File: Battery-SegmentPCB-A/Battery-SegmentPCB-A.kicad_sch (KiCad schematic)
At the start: 10 parts, among them J1 Conn_01x04, J10 Conn_01x16, J2 Conn_01x04, J3 Conn_01x04, J4 Conn_01x04, J5 Conn_01x04, J6 Conn_01x04, J7 Conn_01x04, J8 Conn_01x04, J9 Conn_01x09

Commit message: Initial commit
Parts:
- removed J10: Conn_01x16, footprints:CON_430451612_MOL, symbol Connector_Generic:Conn_01x16
- added J11: Conn_01x09, footprints:CON_436500915_MOL, symbol Connector_Generic:Conn_01x09
- J1, J2, J3, J4, J5, J6, J7, J8: footprint UTSVT_Connectors:Molex_MicroFit3.0_1x4xP3.00mm_PolarizingPeg_Vertical -> footprints:CONN_S4B-PH-K-S_JST
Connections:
- net VOLT1_1 +: now also J11.2 (Pin_2)
- net VOLT1_2 +: now also J11.3 (Pin_3)
- net VOLT1_3 +: now also J11.4 (Pin_4)
- net VOLT1_4 +: now also J11.5 (Pin_5)
- net VOLT1_5 +: now also J11.6 (Pin_6)
- net VOLT1_6 +: now also J11.7 (Pin_7)
- net VOLT1_7 +: now also J11.8 (Pin_8)
- net VOLT1_8 +: now also J11.9 (Pin_9)
- net VOLT_1 -: now also J11.1 (Pin_1)
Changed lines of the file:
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@@
-	(wire
-		(pts
-			(xy 137.16 60.96) (xy 137.16 64.77)
-		)
-		(stroke
-			(width 0)
-			(type default)
-		)
-	)
 	(wire
 		(pts
@@
 	(wire
 		(pts
-			(xy 132.08 60.96) (xy 132.08 64.77)
-		)
-		(stroke
-			(width 0)
-			(type default)
-		)
-	)
-	(wire
-		(pts
 			(xy 33.02 96.52) (xy 38.1 96.52)
 		)
@@
 	(wire
 		(pts
-			(xy 124.46 60.96) (xy 124.46 64.77)
-		)
-		(stroke
-			(width 0)
-			(type default)
-		)
-	)
-	(wire
-		(pts
 			(xy 33.02 62.23) (xy 38.1 62.23)
 		)
@@
 	(wire
 		(pts
-			(xy 139.7 60.96) (xy 139.7 64.77)
-		)
-		(stroke
-			(width 0)
-			(type default)
-		)
-	)
-	(wire
-		(pts
 			(xy 33.02 99.06) (xy 38.1 99.06)
 		)
@@
 	(wire
 		(pts
-			(xy 142.24 60.96) (xy 142.24 64.77)
-		)
-		(stroke
-			(width 0)
-			(type default)
-		)
-	)
-	(wire
-		(pts
-			(xy 134.62 60.96) (xy 134.62 64.77)
-		)
-		(stroke
-			(width 0)
-			(type default)
-		)
-	)
-	(wire
-		(pts
 			(xy 33.02 113.03) (xy 38.1 113.03)
 		)
@@
 	(wire
 		(pts
-			(xy 127 60.96) (xy 127 64.77)
-		)
-		(stroke
-			(width 0)
-			(type default)
-		)
-	)
-	(wire
-		(pts
 			(xy 119.38 60.96) (xy 119.38 64.77)
 		)
@@
 	(wire
 		(pts
-			(xy 129.54 60.96) (xy 129.54 64.77)
+			(xy 101.6 60.96) (xy 101.6 64.77)
 		)
 		(stroke
@@
 			(width 0)
 			(type default)
-		)
-	)
-	(label "VOLT_8 -"
-		(at 142.24 64.77 270)
-		(fields_autoplaced yes)
-		(effects
-			(font
-				(size 1.27 1.27)
-			)
-			(justify right bottom)
 		)
 	)
@@
 	)
 	(label "VOLT_1 -"
-		(at 124.46 64.77 270)
+		(at 101.6 64.77 270)
 		(fields_autoplaced yes)
 		(effects
@@
 		)
 	)
-	(label "VOLT_4 -"
-		(at 132.08 64.77 270)
-		(fields_autoplaced yes)
-		(effects
-			(font
-				(size 1.27 1.27)
-			)
-			(justify right bottom)
-		)
-	)
 	(label "VOLT1_5 +"
 		(at 33.02 78.74 180)
@@
 		)
 	)
-	(label "VOLT_5 -"
-		(at 134.62 64.77 270)
-		(fields_autoplaced yes)
-		(effects
-			(font
-				(size 1.27 1.27)
-			)
-			(justify right bottom)
-		)
-	)
 	(label "TEMP_7"
 		(at 33.02 96.52 180)
@@
 		)
 	)
-	(label "VOLT_3 -"
-		(at 129.54 64.77 270)
-		(fields_autoplaced yes)
-		(effects
-			(font
-				(size 1.27 1.27)
-			)
-			(justify right bottom)
-		)
-	)
 	(label "TEMP_6"
 		(at 33.02 85.09 180)
@@
 		)
 	)
-	(label "VOLT_7 -"
-		(at 139.7 64.77 270)
-		(fields_autoplaced yes)
-		(effects
-			(font
-				(size 1.27 1.27)
-			)
-			(justify right bottom)
-		)
-	)
-	(label "VOLT_2 -"
-		(at 127 64.77 270)
-		(fields_autoplaced yes)
-		(effects
-			(font
-				(size 1.27 1.27)
-			)
-			(justify right bottom)
-		)
-	)
 	(label "VOLT_4 -"
 		(at 33.02 59.69 180)
-		(fields_autoplaced yes)
-		(effects
-			(font
-				(size 1.27 1.27)
-			)
-			(justify right bottom)
-		)
-	)
-	(label "VOLT_6 -"
-		(at 137.16 64.77 270)
 		(fields_autoplaced yes)
 		(effects
@@
 			)
 		)
-		(property "Footprint" "UTSVT_Connectors:Molex_MicroFit3.0_1x4xP3.00mm_PolarizingPeg_Vertical"
+		(property "Footprint" "footprints:CONN_S4B-PH-K-S_JST"
 			(at 43.18 39.37 0)
 			(effects
@@
 			)
 		)
-		(property "Footprint" "UTSVT_Connectors:Molex_MicroFit3.0_1x4xP3.00mm_PolarizingPeg_Vertical"
+		(property "Footprint" "footprints:CONN_S4B-PH-K-S_JST"
 			(at 43.18 27.94 0)
 			(effects
@@
 			)
 		)
-		(property "Footprint" "UTSVT_Connectors:Molex_MicroFit3.0_1x4xP3.00mm_PolarizingPeg_Vertical"
+		(property "Footprint" "footprints:CONN_S4B-PH-K-S_JST"
 			(at 43.18 62.23 0)
 			(effects
@@
 				(path "/4c734560-430e-4436-a585-cee76e7030f6"
 					(reference "J4")
-					(unit 1)
-				)
-			)
-		)
-	)
-	(symbol
-		(lib_id "Connector_Generic:Conn_01x16")
-		(at 121.92 55.88 90)
-		(unit 1)
-		(exclude_from_sim no)
-		(in_bom yes)
-		(on_board yes)
-		(dnp no)
-		(fields_autoplaced yes)
-		(property "Reference" "J10"
-			(at 123.19 49.53 90)
-			(effects
-				(font
-					(size 1.27 1.27)
-				)
-			)
-		)
-		(property "Value" "Conn_01x16"
-			(at 123.19 52.07 90)
-			(effects
-				(font
-					(size 1.27 1.27)
-				)
-			)
-		)
-		(property "Footprint" "footprints:CON_430451612_MOL"
-			(at 121.92 55.88 0)
-			(effects
-				(font
-					(size 1.27 1.27)
-				)
-				(hide yes)
-			)
-		)
-		(property "Datasheet" "~"
-			(at 121.92 55.88 0)
-			(effects
-				(font
-					(size 1.27 1.27)
-				)
-				(hide yes)
-			)
-		)
-		(property "Description" "Generic connector, single row, 01x16, script generated (kicad-library-utils/schlib/autogen/connector/)"
-			(at 121.92 55.88 0)
-			(effects
-				(font
-					(size 1.27 1.27)
-				)
-				(hide yes)
-			)
-		)
-		(pin "16"
-		)
-		(pin "5"
-		)
-		(pin "9"
-		)
-		(pin "2"
-		)
-		(pin "4"
-		)
-		(pin "14"
-		)
-		(pin "6"
-		)
-		(pin "1"
-		)
-		(pin "11"
-		)
-		(pin "10"
-		)
-		(pin "8"
-		)
-		(pin "3"
-		)
-		(pin "13"
-		)
-		(pin "15"
-		)
-		(pin "7"
-		)
-		(pin "12"
-		)
-		(instances
-			(project "Battery-SegmentPCB-A"
-				(path "/4c734560-430e-4436-a585-cee76e7030f6"
-					(reference "J10")
 					(unit 1)
 				)
@@
 			)
 		)
-		(property "Footprint" "UTSVT_Connectors:Molex_MicroFit3.0_1x4xP3.00mm_PolarizingPeg_Vertical"
+		(property "Footprint" "footprints:CONN_S4B-PH-K-S_JST"
 			(at 43.18 107.95 0)
 			(effects
@@
 			)
 		)
-		(property "Footprint" "UTSVT_Connectors:Molex_MicroFit3.0_1x4xP3.00mm_PolarizingPeg_Vertical"
+		(property "Footprint" "footprints:CONN_S4B-PH-K-S_JST"
 			(at 43.18 50.8 0)
 			(effects
@@
 			)
 		)
-		(property "Footprint" "UTSVT_Connectors:Molex_MicroFit3.0_1x4xP3.00mm_PolarizingPeg_Vertical"
+		(property "Footprint" "footprints:CONN_S4B-PH-K-S_JST"
 			(at 43.18 96.52 0)
 			(effects
@@
 			)
 		)
-		(property "Footprint" "UTSVT_Connectors:Molex_MicroFit3.0_1x4xP3.00mm_PolarizingPeg_Vertical"
+		(property "Footprint" "footprints:CONN_S4B-PH-K-S_JST"
 			(at 43.18 73.66 0)
 			(effects
@@
 	)
 	(symbol
+		(lib_id "Connector_Generic:Conn_01x09")
+		(at 111.76 55.88 90)
+		(unit 1)
+		(exclude_from_sim no)
+		(in_bom yes)
+		(on_board yes)
+		(dnp no)
+		(fields_autoplaced yes)
+		(property "Reference" "J11"
+			(at 111.76 49.53 90)
+			(effects
+				(font
+					(size 1.27 1.27)
+				)
+			)
+		)
+		(property "Value" "Conn_01x09"
+			(at 111.76 52.07 90)
+			(effects
+				(font
+					(size 1.27 1.27)
+				)
+			)
+		)
+		(property "Footprint" "footprints:CON_436500915_MOL"
+			(at 111.76 55.88 0)
+			(effects
+				(font
+					(size 1.27 1.27)
+				)
+				(hide yes)
+			)
+		)
+		(property "Datasheet" "~"
+			(at 111.76 55.88 0)
+			(effects
+				(font
+					(size 1.27 1.27)
+				)
+				(hide yes)
+			)
+		)
+		(property "Description" "Generic connector, single row, 01x09, script generated (kicad-library-utils/schlib/autogen/connector/)"
+			(at 111.76 55.88 0)
+			(effects
+				(font
+					(size 1.27 1.27)
+				)
+				(hide yes)
+			)
+		)
+		(pin "2"
+		)
+		(pin "1"
+		)
+		(pin "4"
+		)
+		(pin "3"
+		)
+		(pin "6"
+		)
+		(pin "8"
+		)
+		(pin "5"
+		)
+		(pin "7"
+		)
+		(pin "9"
+		)
+		(instances
+			(project "Battery-SegmentPCB-A"
+				(path "/4c734560-430e-4436-a585-cee76e7030f6"
+					(reference "J11")
+					(unit 1)
+				)
+			)
+		)
+	)
+	(symbol
 		(lib_id "Connector_Generic:Conn_01x04")
 		(at 43.18 85.09 0)
@@
 			)
 		)
-		(property "Footprint" "UTSVT_Connectors:Molex_MicroFit3.0_1x4xP3.00mm_PolarizingPeg_Vertical"
+		(property "Footprint" "footprints:CONN_S4B-PH-K-S_JST"
 			(at 43.18 85.09 0)
 			(effects

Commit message: new template
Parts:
- renumbered J11 to J10
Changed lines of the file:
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@@
 		(dnp no)
 		(fields_autoplaced yes)
-		(property "Reference" "J11"
+		(property "Reference" "J10"
 			(at 111.76 49.53 90)
 			(effects
@@
 			(project "Battery-SegmentPCB-A"
 				(path "/4c734560-430e-4436-a585-cee76e7030f6"
-					(reference "J11")
+					(reference "J10")
 					(unit 1)
 				)

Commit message: started
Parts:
- removed J1, J2, J3, J4, J5, J6, J7, J8: Conn_01x04, footprints:CONN_S4B-PH-K-S_JST, symbol Connector_Generic:Conn_01x04
- added J1, J11, J12, J13, J14, J15, J16, J17, J18, J2, J3, J4, J5, J6, J7, J8: Conn_01x01, MountingHole:MountingHole_3.2mm_M3_DIN965_Pad_TopOnly, symbol Connector_Generic:Conn_01x01
- added J19, J20, J21, J22, J23, J24, J25, J26: Conn_01x02, Connector_Molex:Molex_Nano-Fit_105309-xx02_1x02_P2.50mm_Vertical, symbol Connector_Generic:Conn_01x02
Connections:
- net TEMP_1: now also J19.1 (Pin_1)
- net TEMP_2: now also J20.1 (Pin_1)
- net TEMP_3: now also J21.1 (Pin_1)
- net TEMP_4: now also J22.1 (Pin_1)
- net TEMP_5: now also J23.1 (Pin_1)
- net TEMP_6: now also J24.1 (Pin_1)
- net TEMP_7: now also J25.1 (Pin_1)
- net TEMP_8: now also J26.1 (Pin_1)
- net TEMP_GND: now also J19.2 (Pin_2), J20.2 (Pin_2), J21.2 (Pin_2), J22.2 (Pin_2), J23.2 (Pin_2), J24.2 (Pin_2), J25.2 (Pin_2), J26.2 (Pin_2)
- net VOLT1_1 +: now also J2.1 (Pin_1)
- net VOLT1_2 +: now also J4.1 (Pin_1)
- net VOLT1_3 +: now also J6.1 (Pin_1)
- net VOLT1_4 +: now also J8.1 (Pin_1)
- net VOLT1_5 +: now also J12.1 (Pin_1)
- net VOLT1_6 +: now also J14.1 (Pin_1)
- net VOLT1_7 +: now also J16.1 (Pin_1)
- net VOLT1_8 +: now also J18.1 (Pin_1)
- net VOLT_1 -: now also J1.1 (Pin_1)
- net VOLT_2 -: now also J3.1 (Pin_1)
- net VOLT_3 -: now also J5.1 (Pin_1)
- net VOLT_4 -: now also J7.1 (Pin_1)
- net VOLT_5 -: now also J11.1 (Pin_1)
- net VOLT_6 -: now also J13.1 (Pin_1)
- net VOLT_7 -: now also J15.1 (Pin_1)
- net VOLT_8 -: now also J17.1 (Pin_1)

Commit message: stuff
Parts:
- added F37, F38, F39, F40, F41, F42, F43, F44: PTC Fuse, footprints:FUSC1810X100N, symbol Device:Polyfuse_Small
- J19, J20, J21, J22, J23, J24, J25, J26: footprint Connector_Molex:Molex_Nano-Fit_105309-xx02_1x02_P2.50mm_Vertical -> UTSVT_Connectors:105313-2102
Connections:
- net VOLT1_1 +: now also F37.1; no longer J2.1 (Pin_1)
- net VOLT1_2 +: now also F38.1; no longer J4.1 (Pin_1)
- net VOLT1_3 +: now also F39.1; no longer J6.1 (Pin_1)
- net VOLT1_4 +: now also F40.1; no longer J8.1 (Pin_1)
- net VOLT1_5 +: now also F41.1; no longer J12.1 (Pin_1)
- net VOLT1_6 +: now also F42.1; no longer J14.1 (Pin_1)
- net VOLT1_7 +: now also F43.1; no longer J16.1 (Pin_1)
- net VOLT1_8 +: now also F44.1; no longer J18.1 (Pin_1)
- new net: F44.2, J18.1 (Pin_1)
- new net: F37.2, J2.1 (Pin_1)
- new net: F38.2, J4.1 (Pin_1)
- new net: F39.2, J6.1 (Pin_1)
- new net: F41.2, J12.1 (Pin_1)
- new net: F42.2, J14.1 (Pin_1)
- new net: F43.2, J16.1 (Pin_1)
- new net: F40.2, J8.1 (Pin_1)
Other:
- moved on the sheet: J1, J2, J3, J4, J5, J6, J7, J8

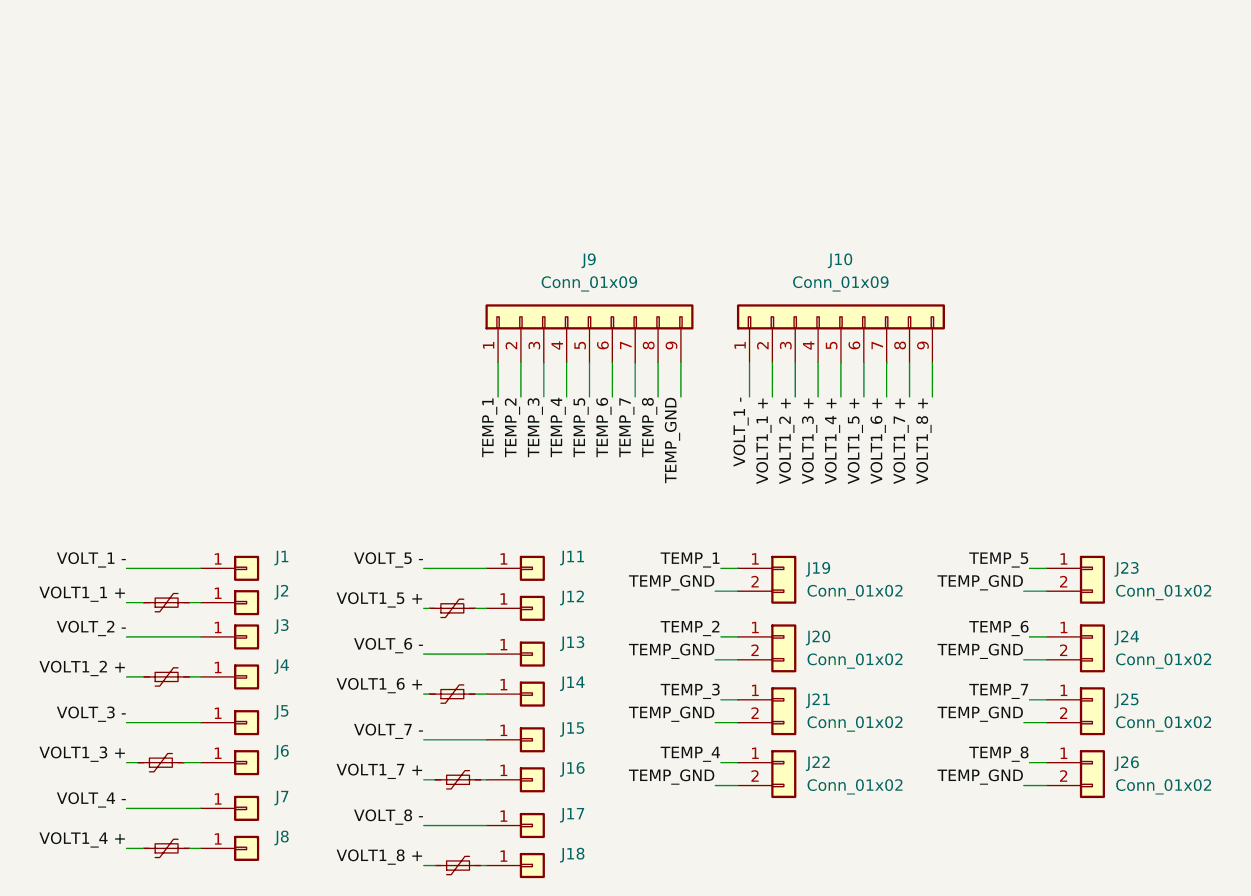
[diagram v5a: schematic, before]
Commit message: seg A, 4 layer, moved conns, flipped fuses, fixed labels
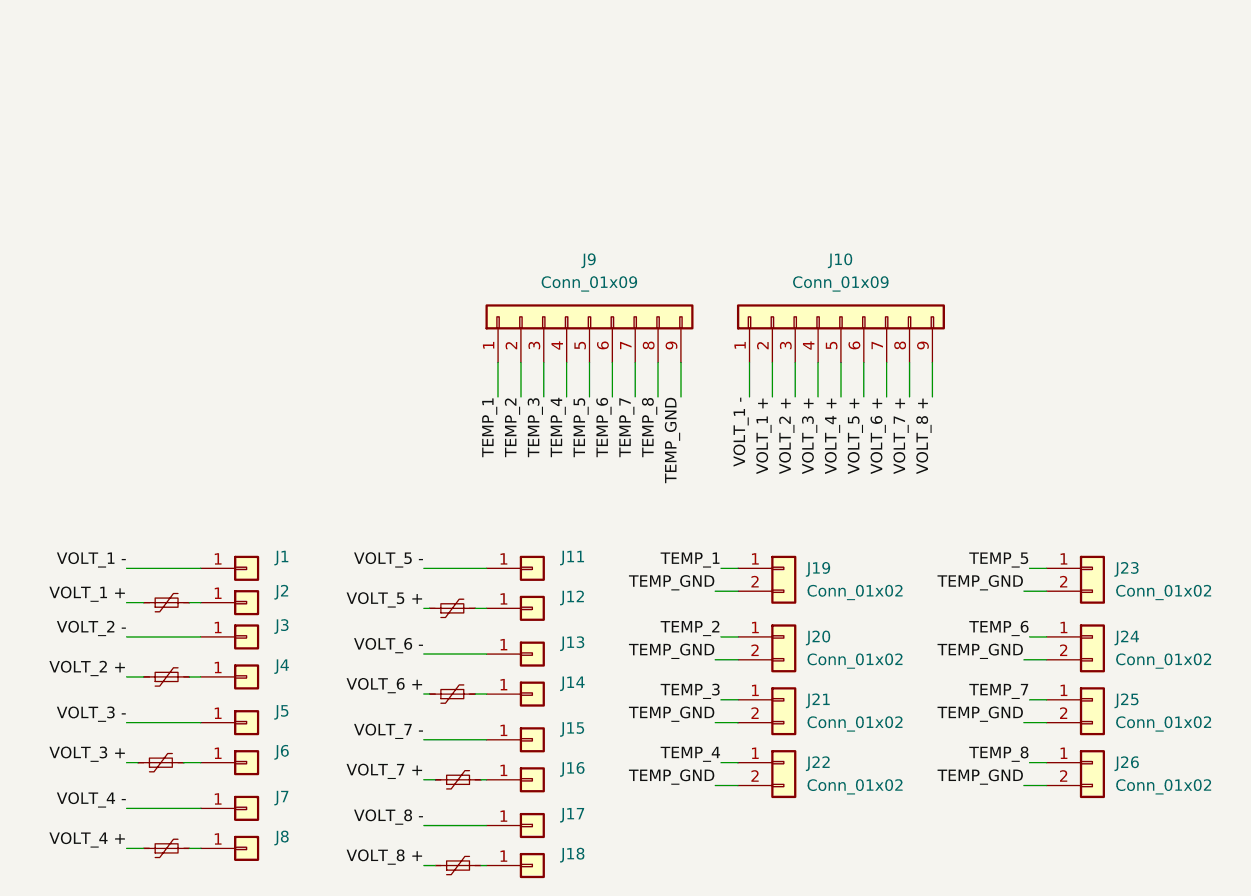
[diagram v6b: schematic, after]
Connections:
- net VOLT1_1 + renamed VOLT_1 +
- net VOLT1_2 + renamed VOLT_2 +
- net VOLT1_3 + renamed VOLT_3 +
- net VOLT1_4 + renamed VOLT_4 +
- net VOLT1_5 + renamed VOLT_5 +
- net VOLT1_6 + renamed VOLT_6 +
- net VOLT1_7 + renamed VOLT_7 +
- net VOLT1_8 + renamed VOLT_8 +
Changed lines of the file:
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@@
 		)
 	)
-	(label "VOLT1_7 +"
+	(label "VOLT_7 +"
 		(at 65.405 107.315 180)
 		(effects
@@
 		)
 	)
-	(label "VOLT1_5 +"
+	(label "VOLT_5 +"
 		(at 114.3 64.77 270)
 		(effects
@@
 		)
 	)
-	(label "VOLT1_2 +"
+	(label "VOLT_2 +"
 		(at 106.68 64.77 270)
 		(effects
@@
 		)
 	)
-	(label "VOLT1_3 +"
+	(label "VOLT_3 +"
 		(at 109.22 64.77 270)
 		(effects
@@
 		)
 	)
-	(label "VOLT1_7 +"
+	(label "VOLT_7 +"
 		(at 119.38 64.77 270)
 		(effects
@@
 		)
 	)
-	(label "VOLT1_2 +"
+	(label "VOLT_2 +"
 		(at 32.385 95.885 180)
 		(effects
@@
 		)
 	)
-	(label "VOLT1_4 +"
+	(label "VOLT_4 +"
 		(at 32.385 114.935 180)
 		(effects
@@
 		)
 	)
-	(label "VOLT1_4 +"
+	(label "VOLT_4 +"
 		(at 111.76 64.77 270)
 		(effects
@@
 		)
 	)
-	(label "VOLT1_6 +"
+	(label "VOLT_6 +"
 		(at 65.405 97.79 180)
 		(effects
@@
 		)
 	)
-	(label "VOLT1_1 +"
+	(label "VOLT_1 +"
 		(at 104.14 64.77 270)
 		(effects
@@
 		)
 	)
-	(label "VOLT1_8 +"
+	(label "VOLT_8 +"
 		(at 65.405 116.84 180)
 		(effects
@@
 		)
 	)
-	(label "VOLT1_1 +"
+	(label "VOLT_1 +"
 		(at 32.385 87.63 180)
 		(effects
@@
 		)
 	)
-	(label "VOLT1_3 +"
+	(label "VOLT_3 +"
 		(at 32.385 105.41 180)
 		(effects
@@
 		)
 	)
-	(label "VOLT1_8 +"
+	(label "VOLT_8 +"
 		(at 121.92 64.77 270)
 		(effects
@@
 		)
 	)
-	(label "VOLT1_6 +"
+	(label "VOLT_6 +"
 		(at 116.84 64.77 270)
 		(effects
@@
 		)
 	)
-	(label "VOLT1_5 +"
+	(label "VOLT_5 +"
 		(at 65.405 88.265 180)
 		(effects
